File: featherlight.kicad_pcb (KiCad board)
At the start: 4 copper layers, 45.7 x 45.7 mm, 92 parts, among them IC1 BNO055, P1 USB_OTG, P2 CONN_01X02, P3 CONN_01X01, P4 CONN_01X01, P5 CONN_01X01, P6 CONN_01X01, SW1 Button, SW2 Button, SW3 Button, SW4 Button, SW5 Button, U1 74AHCT1G125, U2 SAMD21E18A-M, U3 AP2112, U4 MCP73831, Y1 32.768 KHz, Y2 32.768 KHz

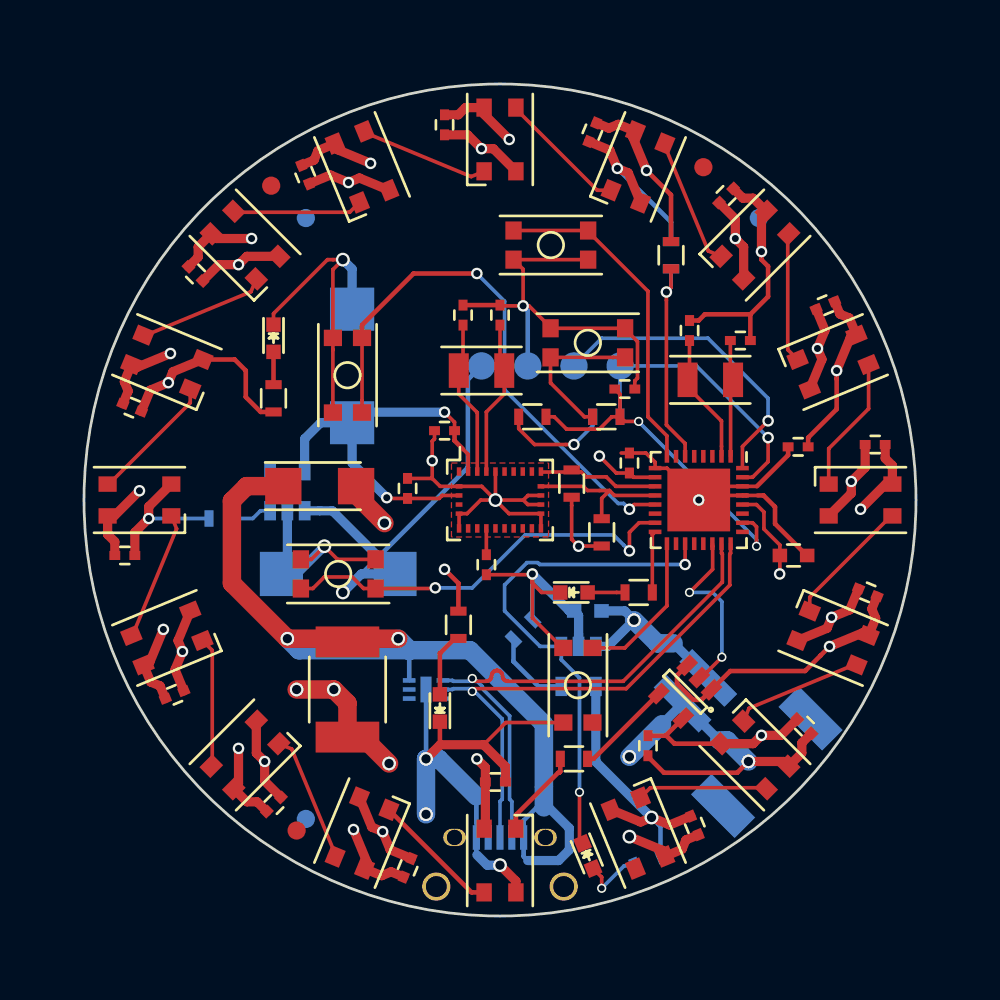
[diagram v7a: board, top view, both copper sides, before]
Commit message: Trying out a 2 inch diameter disk.
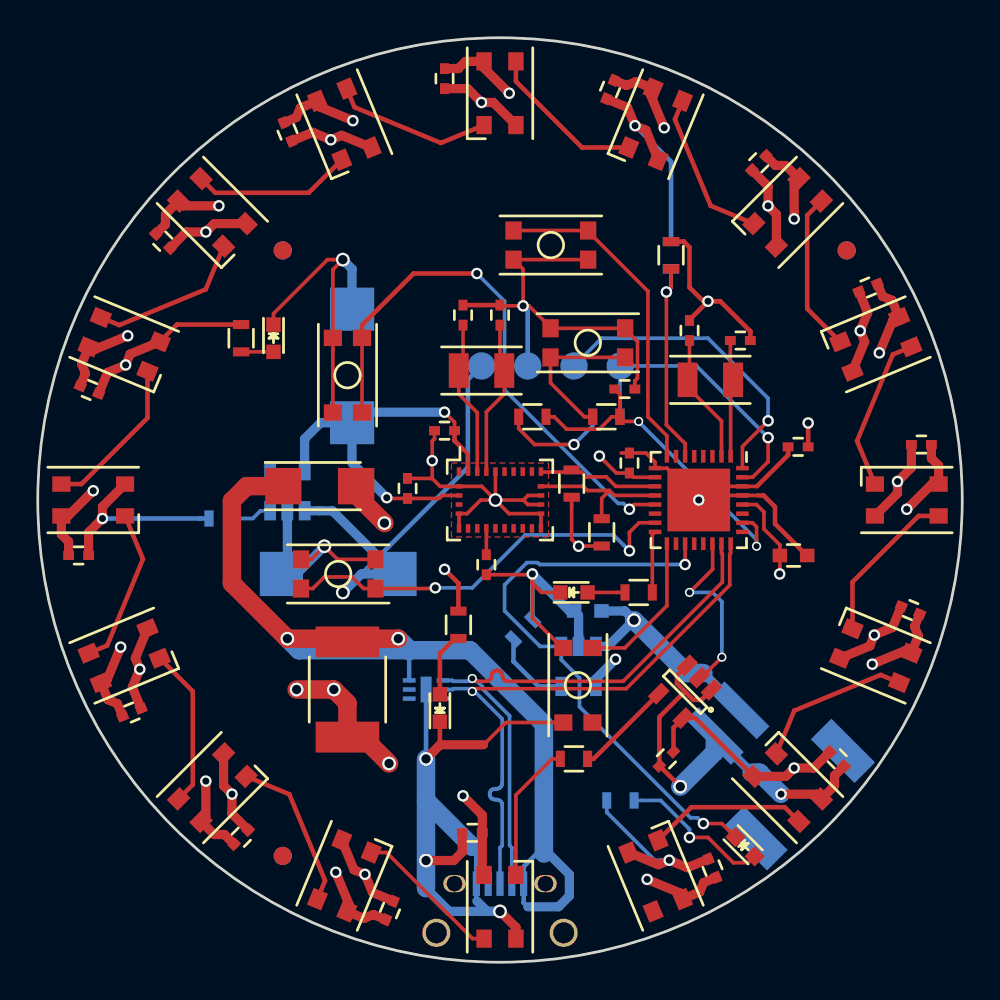
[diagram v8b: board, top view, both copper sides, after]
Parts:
- moved FID2 9.11 mm to (120.7, 87.9)
- moved D21 8.65 mm to (115.1, 120.7), turned to 315 degrees
- moved FID6 5.14 mm to (120.7, 87.9)
- moved R2 3.75 mm to (87.4, 92.7), turned to 270 degrees
- moved R11 3.63 mm to (108.2, 118.1), turned to 0 degrees
- moved FID1 3.61 mm to (89.7, 87.9)
- moved C1 3.07 mm to (100.1, 119.9), turned to 180 degrees
- moved C12 2.54 mm to (121.8, 89.9)
- moved C8 2.54 mm to (89.9, 81.4)
- moved C10 2.54 mm to (107.6, 79.0)
- moved C14 2.54 mm to (124.2, 107.6)
- moved C16 2.54 mm to (113.3, 121.8)
- moved C2 2.54 mm to (95.6, 124.2)
- moved C4 2.54 mm to (81.4, 113.3)
- moved C6 2.54 mm to (79.0, 95.6)
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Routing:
- net GND: track 243.3 -> 237.9 mm, vias 27 -> 29
- net Net-(D21-Pad2): track 3.64 -> 8.45 mm
- net CHARGE_STATUS: track 28.5 -> 32.4 mm
- net D+: track 29.4 -> 32.8 mm
- net Net-(D1-Pad3): track 4.88 -> 7.65 mm
- net D-: track 30.3 -> 32.8 mm
- net VUSB: track 50.7 -> 53.3 mm
- net +BATT: track 30.0 -> 32.5 mm
- net VDD: track 139.3 -> 141.6 mm, vias 20 -> 21
- net /LED Array/D13DO: track 7.08 -> 8.88 mm
- net /LED Array/D5DO: track 7.08 -> 8.88 mm
- net /LED Array/D6DO: track 7.08 -> 8.88 mm
- net /LED Array/D10DO: track 7.08 -> 8.88 mm
- net /LED Array/D2DO: track 7.08 -> 8.88 mm
- net /LED Array/D14DO: track 7.08 -> 8.88 mm
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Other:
- board size 45.7 x 45.7 mm -> 50.8 x 50.8 mm
